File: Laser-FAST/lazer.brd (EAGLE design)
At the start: 140 x 30 mm, 5 parts, among them J1 455-1750-1-ND, J2 455-1750-1-ND, J3 455-1750-1-ND, J4 455-1750-1-ND

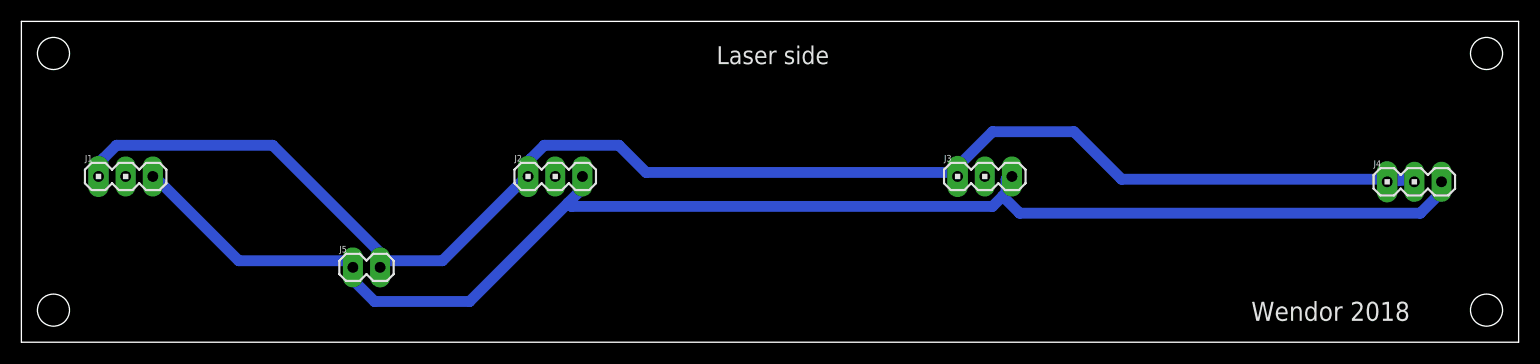
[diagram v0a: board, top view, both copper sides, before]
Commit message: mini board(nano) and lazer-fast pcb modified(DRC errors)
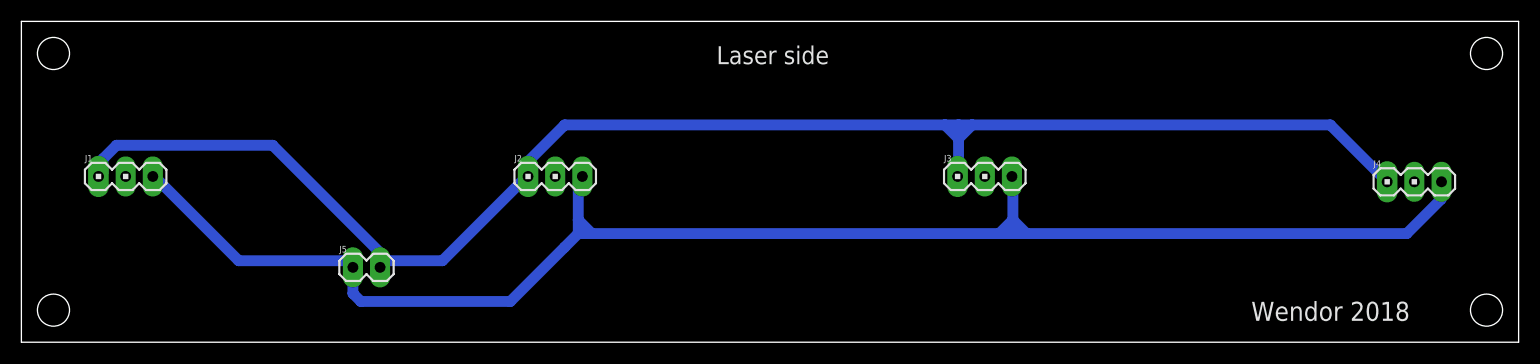
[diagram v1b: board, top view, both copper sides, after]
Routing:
- net GND: track 138.6 -> 149.0 mm
- net POWER: track 144.9 -> 145.9 mm
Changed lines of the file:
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@@
 <wire x1="30.48" y1="7.62" x2="31" y2="7" width="1.016" layer="16"/>
 <wire x1="12.7" y1="15.24" x2="12.29" y2="15.5" width="1.016" layer="16"/>
-<wire x1="52.07" y1="13.97" x2="52.07" y2="15.24" width="1.016" layer="16"/>
-<wire x1="41.91" y1="3.81" x2="51.1175" y2="13.0175" width="1.016" layer="16"/>
-<wire x1="51.1175" y1="13.0175" x2="52.07" y2="13.97" width="1.016" layer="16"/>
-<wire x1="33.02" y1="3.81" x2="41.91" y2="3.81" width="1.016" layer="16"/>
-<wire x1="31.115" y1="5.715" x2="33.02" y2="3.81" width="1.016" layer="16"/>
-<wire x1="31.115" y1="6.985" x2="31.115" y2="5.715" width="1.016" layer="16"/>
-<wire x1="52.07" y1="15.24" x2="52.4566625" y2="15.5" width="1.016" layer="16"/>
-<wire x1="31.115" y1="6.985" x2="31" y2="7" width="1.016" layer="16"/>
-<wire x1="92.075" y1="13.97" x2="92.075" y2="15.24" width="1.016" layer="16"/>
-<wire x1="90.805" y1="12.7" x2="91.7575" y2="13.6525" width="1.016" layer="16"/>
-<wire x1="91.7575" y1="13.6525" x2="92.075" y2="13.97" width="1.016" layer="16"/>
-<wire x1="51.435" y1="12.7" x2="90.805" y2="12.7" width="1.016" layer="16"/>
-<wire x1="92.075" y1="15.24" x2="92.623325" y2="15.5" width="1.016" layer="16"/>
-<wire x1="51.435" y1="12.7" x2="51.1175" y2="13.0175" width="1.016" layer="16"/>
-<wire x1="132.715" y1="13.97" x2="132.715" y2="14.605" width="1.016" layer="16"/>
-<wire x1="130.81" y1="12.065" x2="132.715" y2="13.97" width="1.016" layer="16"/>
-<wire x1="93.345" y1="12.065" x2="130.81" y2="12.065" width="1.016" layer="16"/>
-<wire x1="91.7575" y1="13.6525" x2="93.345" y2="12.065" width="1.016" layer="16"/>
-<wire x1="132.715" y1="14.605" x2="132.7899875" y2="15" width="1.016" layer="16"/>
+<wire x1="31" y1="7" x2="31" y2="4.56" width="1.016" layer="16"/>
+<wire x1="31" y1="4.56" x2="31.75" y2="3.81" width="1.016" layer="16"/>
+<wire x1="31.75" y1="3.81" x2="45.72" y2="3.81" width="1.016" layer="16"/>
+<wire x1="45.72" y1="3.81" x2="50.8" y2="8.89" width="1.016" layer="16"/>
+<wire x1="50.8" y1="8.89" x2="52.07" y2="10.16" width="1.016" layer="16"/>
+<wire x1="129.54" y1="10.16" x2="132.75" y2="13.37" width="1.016" layer="16"/>
+<wire x1="132.75" y1="13.37" x2="132.75" y2="15" width="1.016" layer="16"/>
+<wire x1="52.07" y1="10.16" x2="53.34" y2="10.16" width="1.016" layer="16"/>
+<wire x1="53.34" y1="10.16" x2="91.44" y2="10.16" width="1.016" layer="16"/>
+<wire x1="91.44" y1="10.16" x2="92.71" y2="10.16" width="1.016" layer="16"/>
+<wire x1="92.71" y1="10.16" x2="93.98" y2="10.16" width="1.016" layer="16"/>
+<wire x1="93.98" y1="10.16" x2="129.54" y2="10.16" width="1.016" layer="16"/>
+<wire x1="92.623325" y1="15.5" x2="92.71" y2="15.413325" width="1.016" layer="16"/>
+<wire x1="92.71" y1="15.413325" x2="92.71" y2="11.43" width="1.016" layer="16"/>
+<wire x1="92.71" y1="11.43" x2="92.71" y2="10.16" width="1.016" layer="16"/>
+<wire x1="91.44" y1="10.16" x2="92.71" y2="11.43" width="1.016" layer="16"/>
+<wire x1="92.71" y1="11.43" x2="93.98" y2="10.16" width="1.016" layer="16"/>
+<wire x1="52.4566625" y1="15.5" x2="52.07" y2="15.1133375" width="1.016" layer="16"/>
+<wire x1="52.07" y1="15.1133375" x2="52.07" y2="11.43" width="1.016" layer="16"/>
+<wire x1="52.07" y1="11.43" x2="52.07" y2="10.16" width="1.016" layer="16"/>
+<wire x1="52.07" y1="11.43" x2="53.34" y2="10.16" width="1.016" layer="16"/>
 </signal>
 <signal name="POWER">
@@
 <contactref element="J1" pad="1"/>
 <contactref element="J5" pad="2"/>
-<wire x1="87.75" y1="15.5" x2="87.543325" y2="15.5" width="1.016" layer="16"/>
-<wire x1="127.5" y1="15" x2="127.7099875" y2="15" width="1.016" layer="16"/>
 <wire x1="7.25" y1="15.5" x2="7.21" y2="15.5" width="1.016" layer="16"/>
-<wire x1="102.87" y1="15.24" x2="130.175" y2="15.24" width="1.016" layer="16"/>
-<wire x1="98.425" y1="19.685" x2="102.87" y2="15.24" width="1.016" layer="16"/>
-<wire x1="90.805" y1="19.685" x2="98.425" y2="19.685" width="1.016" layer="16"/>
-<wire x1="86.995" y1="15.875" x2="90.805" y2="19.685" width="1.016" layer="16"/>
-<wire x1="130.175" y1="15.24" x2="127.7099875" y2="15" width="1.016" layer="16"/>
 <wire x1="39.37" y1="7.62" x2="34.29" y2="7.62" width="1.016" layer="16"/>
 <wire x1="34.29" y1="7.62" x2="33.655" y2="7.62" width="1.016" layer="16"/>
@@
 <wire x1="7.62" y1="15.875" x2="7.21" y2="15.5" width="1.016" layer="16"/>
 <wire x1="34.29" y1="7.62" x2="33.54" y2="7" width="1.016" layer="16"/>
-<wire x1="58.42" y1="15.875" x2="86.995" y2="15.875" width="1.016" layer="16"/>
-<wire x1="55.88" y1="18.415" x2="58.42" y2="15.875" width="1.016" layer="16"/>
-<wire x1="48.895" y1="18.415" x2="55.88" y2="18.415" width="1.016" layer="16"/>
-<wire x1="47.625" y1="17.145" x2="48.895" y2="18.415" width="1.016" layer="16"/>
-<wire x1="47.625" y1="15.875" x2="47.625" y2="17.145" width="1.016" layer="16"/>
-<wire x1="86.995" y1="15.875" x2="87.543325" y2="15.5" width="1.016" layer="16"/>
-<wire x1="47.625" y1="15.875" x2="47.3766625" y2="15.5" width="1.016" layer="16"/>
+<wire x1="47.3766625" y1="15.5" x2="47.3766625" y2="16.8966625" width="1.016" layer="16"/>
+<wire x1="47.3766625" y1="16.8966625" x2="50.8" y2="20.32" width="1.016" layer="16"/>
+<wire x1="122.3899875" y1="20.32" x2="127.7099875" y2="15" width="1.016" layer="16"/>
+<wire x1="50.8" y1="20.32" x2="86.36" y2="20.32" width="1.016" layer="16"/>
+<wire x1="86.36" y1="20.32" x2="87.63" y2="20.32" width="1.016" layer="16"/>
+<wire x1="87.63" y1="20.32" x2="88.9" y2="20.32" width="1.016" layer="16"/>
+<wire x1="88.9" y1="20.32" x2="122.3899875" y2="20.32" width="1.016" layer="16"/>
+<wire x1="87.63" y1="20.32" x2="87.63" y2="19.05" width="1.016" layer="16"/>
+<wire x1="87.63" y1="19.05" x2="87.63" y2="15.586675" width="1.016" layer="16"/>
+<wire x1="87.63" y1="15.586675" x2="87.543325" y2="15.5" width="1.016" layer="16"/>
+<wire x1="86.36" y1="20.32" x2="87.63" y2="19.05" width="1.016" layer="16"/>
+<wire x1="87.63" y1="19.05" x2="88.9" y2="20.32" width="1.016" layer="16"/>
 </signal>
 </signals>
